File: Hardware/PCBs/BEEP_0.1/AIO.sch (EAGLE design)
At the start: 89 parts, among them U1 ATXMEGA64D3-AU, U2 TB6612FNG

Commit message: enhance robot case enhance main circuit
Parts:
- removed JP10: (no value), pinhead:PINHD-1X8
- removed U$10, U$11, U$12, U$14, U$15, U$16, U$17, U$18, U$19, U$20, U$6, U$7, U$8, U$9: DMN2075U, BEEP:DMN2075U
- added IC1, IC2: ULN2803ASOP18, BEEP:ULN2803ASOP18
- added JP12: Step_Down_Conn, pinhead:PINHD-1X3
- added JP13: batt_conn, pinhead:PINHD-1X2
- added LED11: (no value), led:LEDCHIPLED_0603
- added R35, R36, R37, R38, R40, R41: 100R, rcl:R-EU_R0402
- added R39: 47K, rcl:R-EU_R0402
- added R42: (no value), rcl:R-EU_R0402
- added S1, S2: (no value), switch-omron:31-XX
- JP11: value (none) -> Color_Conn
- JP9: value (none) -> Motor_Conn; device pinhead:PINHD-1X8 -> pinhead:PINHD-1X4
- R34: value (none) -> 10K
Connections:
- removed net IR_DISTANCE_0: U$12.G
- removed net IR_DISTANCE_1: U$14.G
- removed net IR_DISTANCE_2: U$15.G
- removed net IR_DISTANCE_3: U$16.G
- removed net IR_DISTANCE_4: U$17.G
- removed net IR_DISTANCE_5: U$18.G
- removed net IR_DISTANCE_6: U$19.G
- removed net IR_DISTANCE_7: U$20.G
- removed net LEDA1: U$3.G
- removed net LEDA2: U$2.G
- removed net LEDA3: U$1.G
- removed net LEDK1: U$4.G
- removed net LEDK2: U$5.G
- removed net LEDK3: U$6.G
- removed net LEDK4: U$7.G
- removed net LEDK5: U$8.G
- removed net LEDK6: U$9.G
- removed net LEDK7: U$10.G
- removed net LEDK8: U$11.G
- removed net N$28: R14.1, U$18.S
- removed net N$31: R16.1, U$19.S
- removed net N$37: R18.1, U$20.S
- new net BATT_GND: JP13.2, U$5.S
- new net IR_LED1: IC2.I1
- new net IR_LED2: IC2.I2
- new net IR_LED3: IC2.I3
- new net IR_LED4: IC2.I4
- new net IR_LED5: IC2.I5
- new net IR_LED6: IC2.I6
- new net IR_LED7: IC2.I7
- new net IR_LED8: IC2.I8
- new net IR_PWM: R40.1
- new net LED1: IC1.I1
- new net LED2: IC1.I2
- new net LED3: IC1.I3
- new net LED4: IC1.I4
- new net LED5: IC1.I5
- new net LED6: IC1.I6
- new net LED7: IC1.I7
- new net LED8: IC1.I8
- new net LED_A1: R35.1
- new net LED_A2: R36.1
- new net LED_A3: R37.1
- new net N$38: R35.2, U$3.G
- new net N$39: R36.2, U$2.G
- new net N$40: R37.2, U$1.G
- new net N$41: U$26.5V, U$4.S
- new net N$42: R38.2, R39.1, U$4.G
- new net N$43: IC2.O4, JP4.3
- new net N$44: IC2.O1, JP1.3
- new net N$45: IC2.O2, JP2.3
- new net N$46: IC2.O3, JP3.3
- new net N$47: IC2.O6, JP6.3
- new net N$48: IC2.O5, JP5.3
- new net N$49: IC2.O7, JP7.3
- new net RPI_IKILL: R38.1
- net +3V3: no longer JP10.7
- net +5V: now also JP12.3, R39.2, U$13.D, U$4.D; no longer U$12.D, U$14.D, U$15.D, U$16.D, U$17.D, U$18.D, U$19.D, U$20.D, U$26.5V
- net +7V: now also JP12.1, JP13.1, LED11.A, R41.1; no longer JP10.8
- net GND: now also IC1.GND, IC2.GND, JP12.2, R42.2, S1.S, S2.S, U$5.D; no longer JP10.1, JP10.6, JP9.8, U$10.S, U$11.S, U$13.S, U$4.S, U$5.S, U$6.S, U$7.S, U$8.S, U$9.S
- net IR_LED_PWM: now also R40.2
- net MOTOR_A_IN1: no longer JP9.3
- net MOTOR_A_IN2: no longer JP9.2
- net MOTOR_A_OUT1: now also JP9.4; no longer JP10.5
- net MOTOR_A_OUT2: now also JP9.3; no longer JP10.4
- net MOTOR_A_PWM: no longer JP9.1
- net MOTOR_B_IN1: no longer JP9.5
- net MOTOR_B_IN2: no longer JP9.6
- net MOTOR_B_OUT1: now also JP9.1; no longer JP10.2
- net MOTOR_B_OUT2: now also JP9.2; no longer JP10.3
- net MOTOR_B_PWM: no longer JP9.7
- net MOTOR_STBY: no longer JP9.4
- net N$10: now also IC1.O4; no longer U$7.D
- net N$12: now also R10.1, R12.1, R14.1, R16.1, R18.1, R4.1, R8.1, U$13.S; no longer U$14.S
- net N$13: now also IC2.O8; no longer JP1.3, JP2.3, JP3.3, JP4.3, JP5.3, JP6.3, JP7.3, U$13.D
- net N$14: now also IC1.O5; no longer U$8.D
- net N$15: now also IC1.O6; no longer U$9.D
- net N$16: now also IC1.O7; no longer U$10.D
- net N$17: now also IC1.O8; no longer U$11.D
- net N$19: now also LED11.C, R42.1; no longer R8.1, U$15.S
- net N$22: now also S1.P, U$26.GPIO_23; no longer R10.1, U$16.S
- net N$25: now also S2.P, U$26.GPIO_22; no longer R12.1, U$17.S
- net N$4: now also IC1.O2; no longer U$5.D
- net N$6: now also IC1.O1; no longer U$4.D
- net N$7: now also IC1.O3; no longer U$6.D
- net N$8: now also R41.2, U$5.G; no longer R4.1, U$12.S
- net SCL: now also U$26.GPIO_1
- net SDA: now also U$26.GPIO_0
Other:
- note added: "IR Distance"
- note added: "PDI Interface"
- note added: "RGB LEDs"
- note added: "Rev Batt Protection"
- moved on the sheet: LED1, LED10, LED2, LED3, LED4, LED5, LED6, LED7, LED8, LED9, R1, R2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

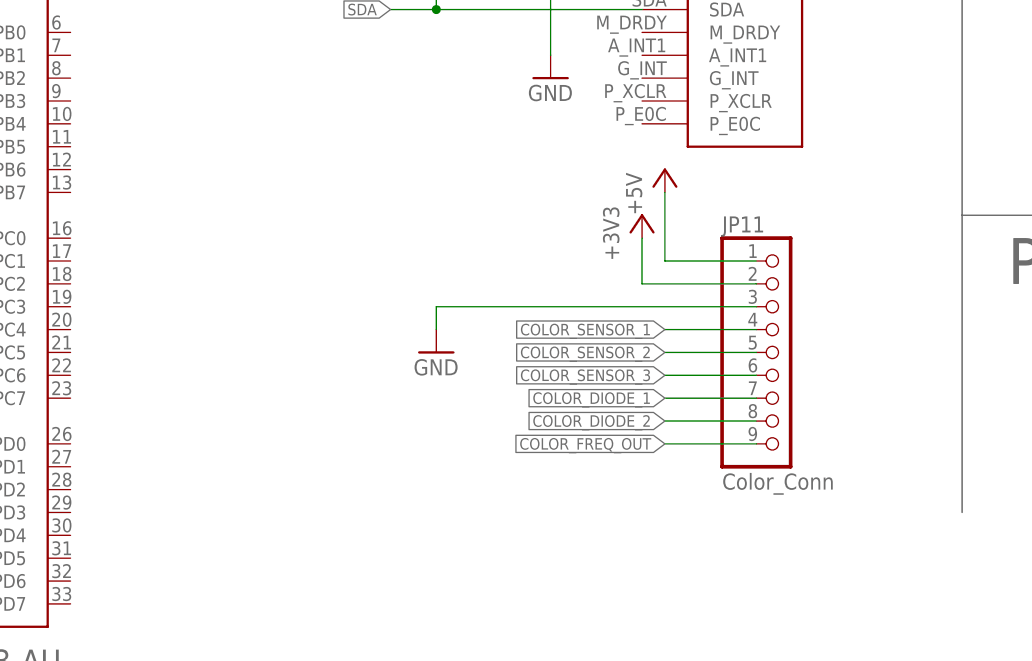
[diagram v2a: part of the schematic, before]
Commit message: add robot pcb space to eagle pcb enhance circuit
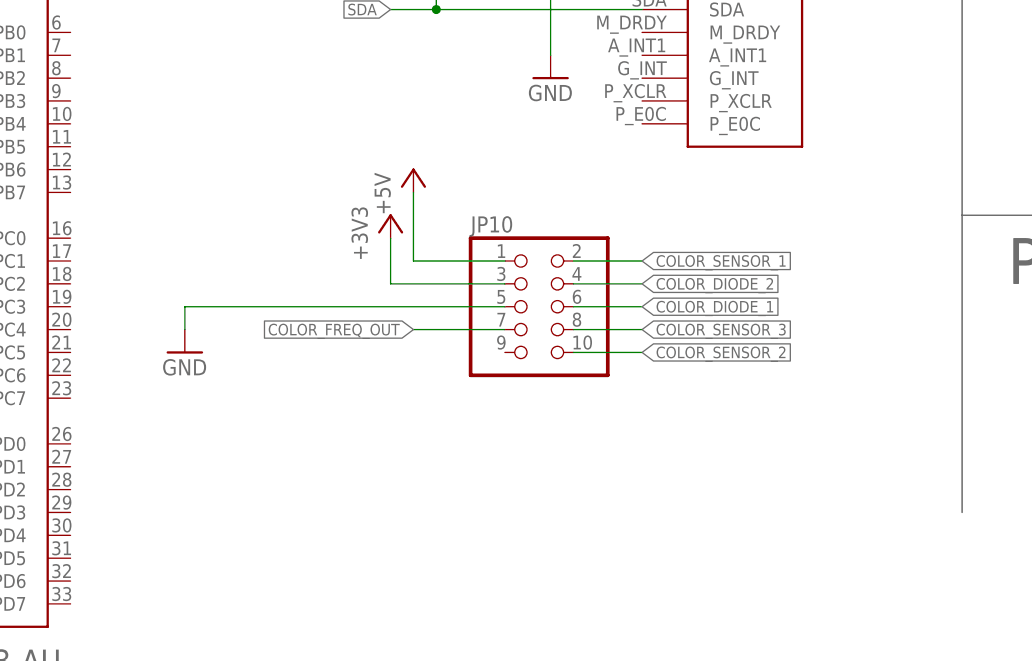
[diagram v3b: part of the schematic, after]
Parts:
- removed JP11: Color_Conn, pinhead:PINHD-1X9
- added JP10: (no value), pinhead:PINHD-2X5
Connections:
- net +3V3: now also JP10.3; no longer JP11.2
- net +5V: now also JP10.1; no longer JP11.1
- net COLOR_DIODE_1: now also JP10.6; no longer JP11.7
- net COLOR_DIODE_2: now also JP10.4; no longer JP11.8
- net COLOR_FREQ_OUT: now also JP10.7; no longer JP11.9
- net COLOR_SENSOR_1: now also JP10.2; no longer JP11.4
- net COLOR_SENSOR_2: now also JP10.10; no longer JP11.5
- net COLOR_SENSOR_3: now also JP10.8; no longer JP11.6
- net GND: now also JP10.5; no longer JP11.3
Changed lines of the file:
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@@
 <part name="R34" library="rcl" deviceset="R-EU_" device="R0402" value="10K"/>
 <part name="FRAME4" library="frames" deviceset="A4L-LOC" device=""/>
-<part name="JP11" library="pinhead" deviceset="PINHD-1X9" device="" value="Color_Conn"/>
 <part name="+3V22" library="supply1" deviceset="+3V3" device=""/>
 <part name="P+15" library="supply1" deviceset="+5V" device=""/>
@@
 <part name="JP9" library="pinhead" deviceset="PINHD-1X4" device="" value="Motor_Conn"/>
 <part name="GND5" library="supply1" deviceset="GND" device=""/>
+<part name="JP10" library="pinhead" deviceset="PINHD-2X5" device=""/>
 </parts>
 <sheets>
@@
 <instance part="R34" gate="G$1" x="63.5" y="137.16" rot="R270"/>
 <instance part="FRAME4" gate="G$1" x="12.7" y="25.4"/>
-<instance part="JP11" gate="A" x="185.42" y="68.58"/>
-<instance part="+3V22" gate="G$1" x="170.18" y="83.82"/>
-<instance part="P+15" gate="1" x="172.72" y="88.9"/>
-<instance part="GND38" gate="1" x="147.32" y="68.58"/>
+<instance part="+3V22" gate="G$1" x="142.24" y="83.82"/>
+<instance part="P+15" gate="1" x="144.78" y="88.9"/>
+<instance part="GND38" gate="1" x="119.38" y="68.58"/>
 <instance part="IC1" gate="IC" x="200.66" y="281.94" rot="R90"/>
 <instance part="GND1" gate="1" x="215.9" y="261.62"/>
@@
 <instance part="JP9" gate="A" x="365.76" y="71.12" rot="R180"/>
 <instance part="GND5" gate="1" x="160.02" y="160.02"/>
+<instance part="JP10" gate="A" x="157.48" y="73.66"/>
 </instances>
 <busses>
@@
 </segment>
 <segment>
-<pinref part="JP11" gate="A" pin="3"/>
 <pinref part="GND38" gate="1" pin="GND"/>
-<wire x1="182.88" y1="73.66" x2="147.32" y2="73.66" width="0.1524" layer="91"/>
-<wire x1="147.32" y1="73.66" x2="147.32" y2="71.12" width="0.1524" layer="91"/>
+<wire x1="154.94" y1="73.66" x2="119.38" y2="73.66" width="0.1524" layer="91"/>
+<wire x1="119.38" y1="73.66" x2="119.38" y2="71.12" width="0.1524" layer="91"/>
+<pinref part="JP10" gate="A" pin="5"/>
 </segment>
 <segment>
@@
 </segment>
 <segment>
-<pinref part="JP11" gate="A" pin="1"/>
-<wire x1="182.88" y1="78.74" x2="172.72" y2="78.74" width="0.1524" layer="91"/>
+<wire x1="154.94" y1="78.74" x2="144.78" y2="78.74" width="0.1524" layer="91"/>
 <pinref part="P+15" gate="1" pin="+5V"/>
-<wire x1="172.72" y1="78.74" x2="172.72" y2="86.36" width="0.1524" layer="91"/>
+<wire x1="144.78" y1="78.74" x2="144.78" y2="86.36" width="0.1524" layer="91"/>
+<pinref part="JP10" gate="A" pin="1"/>
 </segment>
 <segment>
@@
 </segment>
 <segment>
-<pinref part="JP11" gate="A" pin="2"/>
-<wire x1="182.88" y1="76.2" x2="170.18" y2="76.2" width="0.1524" layer="91"/>
+<wire x1="154.94" y1="76.2" x2="142.24" y2="76.2" width="0.1524" layer="91"/>
 <pinref part="+3V22" gate="G$1" pin="+3V3"/>
-<wire x1="170.18" y1="76.2" x2="170.18" y2="81.28" width="0.1524" layer="91"/>
+<wire x1="142.24" y1="76.2" x2="142.24" y2="81.28" width="0.1524" layer="91"/>
+<pinref part="JP10" gate="A" pin="3"/>
 </segment>
 <segment>
@@
 <net name="COLOR_SENSOR_1" class="0">
 <segment>
-<pinref part="JP11" gate="A" pin="4"/>
-<wire x1="182.88" y1="71.12" x2="172.72" y2="71.12" width="0.1524" layer="91"/>
-<label x="172.72" y="71.12" size="1.27" layer="95" rot="R180" xref="yes"/>
+<wire x1="162.56" y1="78.74" x2="170.18" y2="78.74" width="0.1524" layer="91"/>
+<label x="170.18" y="78.74" size="1.27" layer="95" xref="yes"/>
+<pinref part="JP10" gate="A" pin="2"/>
 </segment>
 </net>
 <net name="COLOR_SENSOR_2" class="0">
 <segment>
-<pinref part="JP11" gate="A" pin="5"/>
-<wire x1="182.88" y1="68.58" x2="172.72" y2="68.58" width="0.1524" layer="91"/>
-<label x="172.72" y="68.58" size="1.27" layer="95" rot="R180" xref="yes"/>
+<wire x1="162.56" y1="68.58" x2="170.18" y2="68.58" width="0.1524" layer="91"/>
+<label x="170.18" y="68.58" size="1.27" layer="95" xref="yes"/>
+<pinref part="JP10" gate="A" pin="10"/>
 </segment>
 </net>
 <net name="COLOR_SENSOR_3" class="0">
 <segment>
-<pinref part="JP11" gate="A" pin="6"/>
-<wire x1="182.88" y1="66.04" x2="172.72" y2="66.04" width="0.1524" layer="91"/>
-<label x="172.72" y="66.04" size="1.27" layer="95" rot="R180" xref="yes"/>
+<wire x1="162.56" y1="71.12" x2="170.18" y2="71.12" width="0.1524" layer="91"/>
+<label x="170.18" y="71.12" size="1.27" layer="95" xref="yes"/>
+<pinref part="JP10" gate="A" pin="8"/>
 </segment>
 </net>
 <net name="COLOR_DIODE_1" class="0">
 <segment>
-<pinref part="JP11" gate="A" pin="7"/>
-<wire x1="182.88" y1="63.5" x2="172.72" y2="63.5" width="0.1524" layer="91"/>
-<label x="172.72" y="63.5" size="1.27" layer="95" rot="R180" xref="yes"/>
+<wire x1="162.56" y1="73.66" x2="170.18" y2="73.66" width="0.1524" layer="91"/>
+<label x="170.18" y="73.66" size="1.27" layer="95" xref="yes"/>
+<pinref part="JP10" gate="A" pin="6"/>
 </segment>
 </net>
 <net name="COLOR_DIODE_2" class="0">
 <segment>
-<pinref part="JP11" gate="A" pin="8"/>
-<wire x1="182.88" y1="60.96" x2="172.72" y2="60.96" width="0.1524" layer="91"/>
-<label x="172.72" y="60.96" size="1.27" layer="95" rot="R180" xref="yes"/>
+<wire x1="162.56" y1="76.2" x2="170.18" y2="76.2" width="0.1524" layer="91"/>
+<label x="170.18" y="76.2" size="1.27" layer="95" xref="yes"/>
+<pinref part="JP10" gate="A" pin="4"/>
 </segment>
 </net>
 <net name="COLOR_FREQ_OUT" class="0">
 <segment>
-<pinref part="JP11" gate="A" pin="9"/>
-<wire x1="182.88" y1="58.42" x2="172.72" y2="58.42" width="0.1524" layer="91"/>
-<label x="172.72" y="58.42" size="1.27" layer="95" rot="R180" xref="yes"/>
-</segment>
-</net>
+<wire x1="154.94" y1="71.12" x2="144.78" y2="71.12" width="0.1524" layer="91"/>
+<label x="144.78" y="71.12" size="1.27" layer="95" rot="R180" xref="yes"/>
+<pinref part="JP10" gate="A" pin="7"/>
+</segment>
+</net>

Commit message: enhance BEEP main pcb, rgb and ir boards
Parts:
- removed JP1, JP2, JP3, JP4, JP5, JP6, JP7, JP8: (no value), pinhead:PINHD-2X2/90
- removed JP10: (no value), pinhead:PINHD-2X5
- removed JP9: Motor_Conn, pinhead:PINHD-1X4
- removed LED1, LED2, LED3, LED4, LED5, LED6, LED7, LED8: F503605050, BEEP:F503605050
- removed R10, R11, R12, R13, R14, R15, R16, R17, R18, R19, R4, R5, R6, R7, R8, R9: (no value), rcl:R-EU_R0402
- removed R40: 100R, rcl:R-EU_R0402
- removed U$13: DMN2075U, BEEP:DMN2075U
- added C6, C7, C8, C9: 100nF, rcl:C-EUC0603
- added U$8: DMN2075U, BEEP:DMN2075U
- added X1, X2, X3, X4, X5, X6, X7, X8: MICROMATCH-8, Con-amp-micromatch:MICROMATCH-8
- added X10: MICROMATCH-10, Con-amp-micromatch:MICROMATCH-10
- added X9: MICROMATCH-4, Con-amp-micromatch:MICROMATCH-4
- C1, C3, C5: device rcl:C-EUC0402 -> rcl:C-EUC0603
- C2, C4: device rcl:C-USC0402 -> rcl:C-USC1812
- R1, R2, R20, R21, R22, R23, R24, R25, R26, R27, R28, R29, R3, R30, R31, R32, R33, R34, R35, R36, R37, R38, R39, R41, R42: device rcl:R-EU_R0402 -> rcl:R-EU_R0603
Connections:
- net IR_LED1 renamed IR_LED_K0
- net IR_LED2 renamed IR_LED_K1
- net IR_LED3 renamed IR_LED_K2
- net IR_LED4 renamed IR_LED_K3
- net IR_LED5 renamed IR_LED_K4
- net IR_LED6 renamed IR_LED_K5
- net IR_LED7 renamed IR_LED_K6
- net IR_LED8 renamed IR_LED_K7
- net LED1 renamed LED_K0
- net LED2 renamed LED_K1
- net LED3 renamed LED_K2
- net LED4 renamed LED_K3
- net LED5 renamed LED_K4
- net LED6 renamed LED_K5
- net LED7 renamed LED_K6
- net LED8 renamed LED_K7
- removed net ADISTANCE0: JP1.4, R5.2
- removed net ADISTANCE1: JP2.4, R7.2
- removed net ADISTANCE2: JP3.4, R9.2
- removed net ADISTANCE3: JP4.4, R11.2
- removed net ADISTANCE4: JP5.4, R13.2
- removed net ADISTANCE5: JP6.4, R15.2
- removed net ADISTANCE6: JP7.4, R17.2
- removed net ADISTANCE7: JP8.4, R19.2
- removed net IR_LED_PWM: R40.2, U$13.G
- removed net IR_PWM: R40.1
- removed net LED_A3: R37.1
- removed net N$10: IC1.O4, LED4.BC, LED4.GC, LED4.RC
- removed net N$12: R10.1, R12.1, R14.1, R16.1, R18.1, R4.1, R6.1, R8.1, U$13.S
- removed net N$13: IC2.O8, JP8.3
- removed net N$14: IC1.O5, LED5.BC, LED5.GC, LED5.RC
- removed net N$15: IC1.O6, LED6.BC, LED6.GC, LED6.RC
- removed net N$16: IC1.O7, LED7.BC, LED7.GC, LED7.RC
- removed net N$17: IC1.O8, LED8.BC, LED8.GC, LED8.RC
- removed net N$18: JP3.1, R8.2
- removed net N$21: JP4.1, R10.2
- removed net N$24: JP5.1, R12.2
- removed net N$27: JP6.1, R14.2
- removed net N$30: JP7.1, R16.2
- removed net N$33: LED1.RA, LED2.RA, LED3.RA, LED4.RA, LED5.RA, LED6.RA, LED7.RA, LED8.RA, R1.2
- removed net N$34: LED1.GA, LED2.GA, LED3.GA, LED4.GA, LED5.GA, LED6.GA, LED7.GA, LED8.GA, R2.2
- removed net N$35: LED1.BA, LED2.BA, LED3.BA, LED4.BA, LED5.BA, LED6.BA, LED7.BA, LED8.BA, R3.2
- removed net N$36: JP8.1, R18.2
- removed net N$4: IC1.O2, LED2.BC, LED2.GC, LED2.RC
- removed net N$43: IC2.O4, JP4.3
- removed net N$44: IC2.O1, JP1.3
- removed net N$45: IC2.O2, JP2.3
- removed net N$46: IC2.O3, JP3.3
- removed net N$47: IC2.O6, JP6.3
- removed net N$48: IC2.O5, JP5.3
- removed net N$49: IC2.O7, JP7.3
- removed net N$6: IC1.O1, LED1.BC, LED1.GC, LED1.RC
- removed net N$7: IC1.O3, LED3.BC, LED3.GC, LED3.RC
- removed net N$9: JP2.1, R6.2
- new net ADISTANCE_0: X4-7.S
- new net ADISTANCE_1: X1-7.S
- new net ADISTANCE_2: X2-7.S
- new net ADISTANCE_3: X3-7.S
- new net ADISTANCE_4: X5-7.S
- new net ADISTANCE_5: X6-7.S
- new net ADISTANCE_6: X7-7.S
- new net ADISTANCE_7: X8-7.S
- new net COLOR_SENSOR_PWM_LED: U$8.G
- new net IR_LED_K0_OUT: IC2.O1, X4-5.S
- new net IR_LED_K1_OUT: IC2.O2, X1-5.S
- new net IR_LED_K2_OUT: IC2.O3, X2-5.S
- new net IR_LED_K3_OUT: IC2.O4, X3-5.S
- new net IR_LED_K4_OUT: IC2.O5, X5-5.S
- new net IR_LED_K5_OUT: IC2.O6, X6-5.S
- new net IR_LED_K6_OUT: IC2.O7, X7-5.S
- new net IR_LED_K7_OUT: IC2.O8, X8-5.S
- new net LED_A0: R35.1
- new net LED_A0_OUT: R3.2, X1-1.S, X2-1.S, X3-1.S, X4-1.S, X5-1.S, X6-1.S, X7-1.S, X8-1.S
- new net LED_A1_OUT: R2.2, X1-2.S, X2-2.S, X3-2.S, X4-2.S, X5-2.S, X6-2.S, X7-2.S, X8-2.S
- new net LED_A2_OUT: R1.2, X1-3.S, X2-3.S, X3-3.S, X4-3.S, X5-3.S, X6-3.S, X7-3.S, X8-3.S
- new net LED_K0_OUT: IC1.O1, X4-4.S
- new net LED_K1_OUT: IC1.O2, X1-4.S
- new net LED_K2_OUT: IC1.O3, X2-4.S
- new net LED_K3_OUT: IC1.O4, X3-4.S
- new net LED_K4_OUT: IC1.O5, X5-4.S
- new net LED_K5_OUT: IC1.O6, X6-4.S
- new net LED_K6_OUT: IC1.O7, X7-4.S
- new net LED_K7_OUT: IC1.O8, X8-4.S
- net +3V3: now also C5.2, C6.2, C7.2, C8.2, C9.2, X10-10.S; no longer JP1.2, JP10.3, JP2.2, JP3.2, JP4.2, JP5.2, JP6.2, JP7.2, JP8.2
- net +5V: now also U$8.D, X1-8.S, X2-8.S, X3-8.S, X4-8.S, X5-8.S, X6-8.S, X7-8.S, X8-8.S; no longer JP10.1, U$13.D
- net COLOR_DIODE_1: now also X10-4.S; no longer JP10.6
- net COLOR_DIODE_2: now also X10-3.S; no longer JP10.4
- net COLOR_FREQ_OUT: now also X10-7.S; no longer JP10.7
- net COLOR_SENSOR_1: now also X10-2.S; no longer JP10.2
- net COLOR_SENSOR_2: now also X10-6.S; no longer JP10.10
- net COLOR_SENSOR_3: now also X10-5.S; no longer JP10.8
- net GND: now also C5.1, C6.1, C7.1, C8.1, C9.1, X1-6.S, X10-8.S, X2-6.S, X3-6.S, X4-6.S, X5-6.S, X6-6.S, X7-6.S, X8-6.S; no longer JP10.5, R11.1, R13.1, R15.1, R17.1, R19.1, R5.1, R7.1, R9.1
- net LED_A1: now also R36.1; no longer R35.1
- net LED_A2: now also R37.1; no longer R36.1
- net MOTOR_A_OUT1: now also X9-1.S; no longer JP9.4
- net MOTOR_A_OUT2: now also X9-2.S; no longer JP9.3
- net MOTOR_B_OUT1: now also X9-4.S; no longer JP9.1
- net MOTOR_B_OUT2: now also X9-3.S; no longer JP9.2
- net N$5: now also U$8.S, X10-9.S; no longer JP1.1, R4.2
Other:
- note added: "Batt Connector"
- note added: "Batt Step Down"
- note added: "Kill RPI on low batt"
- note added: "LOW BATT Protection"
- note added: "RGB LEDs & IR distance sensors"
- note added: "Raspberry Pi"
- note removed: "IR Distance"
- note removed: "RGB LEDs"
- moved on the sheet: C5, IC1, IC2, JP12, JP13, LED10, LED11, LED9, R1, R2, R28, R29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

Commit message: continue working on shematic for AIO BEEP started with pcb routing
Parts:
- added C10, C11, C12: 100nF, rcl:C-EUC0603
- added IC3, IC4: 74HC238D, BEEP:74HC238D
- added R10, R11, R6, R7, R8, R9: (no value), rcl:R-EU_R0603
- added R4, R5: 10K, rcl:R-EU_R0603
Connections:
- removed net BATT_WARN_2: LED9.A
- removed net IR_LED_K2: IC2.I3
- removed net IR_LED_K3: IC2.I4
- removed net IR_LED_K4: IC2.I5
- removed net IR_LED_K5: IC2.I6
- removed net IR_LED_K6: IC2.I7
- removed net IR_LED_K7: IC2.I8
- removed net LED_K0: IC1.I1
- removed net LED_K1: IC1.I2
- removed net LED_K2: IC1.I3
- removed net LED_K3: IC1.I4
- removed net LED_K4: IC1.I5
- removed net LED_K5: IC1.I6
- removed net LED_K6: IC1.I7
- removed net LED_K7: IC1.I8
- removed net PDI_CLOCK: R34.2, U1.!RESET!/PDI
- new net BATT_WARN_0: R31.1, U1.PA3
- new net IR_LED_MK0: IC3.A, U1.PF2
- new net IR_LED_MK1: IC3.B, U1.PF1
- new net IR_LED_MK2: IC3.C, U1.PF0
- new net N$10: IC2.I6, IC3.Y5
- new net N$12: IC2.I7, IC3.Y6
- new net N$13: IC2.I8, IC3.Y7
- new net N$14: IC3.G2A, R7.2
- new net N$15: IC3.G2B, R6.2
- new net N$16: IC3.G1, R8.1
- new net N$17: IC4.G2A, R10.2
- new net N$18: IC4.G2B, R9.2
- new net N$21: IC1.I1, IC4.Y0
- new net N$24: IC1.I2, IC4.Y1
- new net N$27: IC1.I3, IC4.Y2
- new net N$28: IC1.I4, IC4.Y3
- new net N$30: IC1.I5, IC4.Y4
- new net N$31: IC1.I6, IC4.Y5
- new net N$33: IC1.I7, IC4.Y6
- new net N$34: IC1.I8, IC4.Y7
- new net N$35: IC4.G1, R11.1
- new net N$4: R4.1, R5.2, U1.PA0
- new net N$6: IC2.I3, IC3.Y2
- new net N$7: IC2.I4, IC3.Y3
- new net N$9: IC2.I5, IC3.Y4
- new net RGB_LED_MK0: IC4.A, U1.PF5
- new net RGB_LED_MK1: IC4.B, U1.PF4
- new net RGB_LED_MK2: IC4.C, U1.PF3
- net +3V3: now also C10.2, C11.2, C12.2, IC3.VCC, IC4.VCC, R11.2, R5.1, R8.2, U1.AVCC
- net ADISTANCE_0: now also U1.PB0
- net ADISTANCE_1: now also U1.PB1
- net ADISTANCE_2: now also U1.PB2
- net ADISTANCE_3: now also U1.PB3
- net ADISTANCE_4: now also U1.PB4
- net ADISTANCE_5: now also U1.PB5
- net ADISTANCE_6: now also U1.PB6
- net ADISTANCE_7: now also U1.PB7
- net BATT_VOLTAGE: now also U1.PA2
- net BATT_WARN_1: now also R30.1, U1.PA4; no longer LED10.A
- net COLOR_DIODE_1: now also U1.PE5
- net COLOR_DIODE_2: now also U1.PE6
- net COLOR_FREQ_OUT: now also U1.PE2
- net COLOR_SENSOR_1: now also U1.PE7
- net COLOR_SENSOR_2: now also U1.PE3
- net COLOR_SENSOR_3: now also U1.PE4
- net COLOR_SENSOR_PWM_LED: now also U1.PC3
- net GND: now also C10.1, C11.1, C12.1, IC3.GND, IC4.GND, LED10.C, LED9.C, R10.1, R4.2, R6.1, R7.1, R9.1, U1.PA1; no longer R30.2, R31.2
- net IR_LED_K0: now also IC3.Y0
- net IR_LED_K1: now also IC3.Y1
- net LED_A0: now also U1.PC0
- net LED_A1: now also U1.PC1
- net LED_A2: now also U1.PC2
- net MOTOR_A_IN1: now also U1.PD4
- net MOTOR_A_IN2: now also U1.PD7
- net MOTOR_A_PWM: now also U1.PC4
- net MOTOR_B_IN1: now also U1.PD5
- net MOTOR_B_IN2: now also U1.PD6
- net MOTOR_B_PWM: now also U1.PC5
- net MOTOR_STBY: now also U1.PC6
- net N$29: now also LED9.A, R30.2; no longer LED9.C, R30.1
- net N$32: now also LED10.A, R31.2; no longer LED10.C, R31.1
- net PDI_CLK: now also R34.2, U1.!RESET!/PDI
- net RPI_IKILL: now also U1.PD0
- net RPI_RX: now also U1.PD3
- net RPI_TX: now also U1.PD2
- net SCL: now also U1.PE1
- net SDA: now also U1.PE0
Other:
- moved on the sheet: C1, C2, C3, C4, IC1, IC2, JP12, JP13, LED10, LED11, LED9, R1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
